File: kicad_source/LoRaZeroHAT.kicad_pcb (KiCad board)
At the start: 2 copper layers, 28 x 87 mm, 69 parts, among them J1 USB_B_Micro, J2 BM04B-SRSS-TB, Q1 NTR4171P, SW1 SW_Push, SW2 SW_Push, SW3 SW_SPDT, U1 RP2040, U2 Ai-Thinker-Ra-01, U3 NEO-M8N, U4 W25Q16JVSS, U5 24LC32, U6 BME280, U7 TPS3839DBZ, U8 TPS73630DBV, U9 MCP73832-2-OT, Y1 Crystal_GND24_Small

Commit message: connected schematic to layout
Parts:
- removed BT1: Battery_Cell, generationmake:KEYSTONE_1043
- removed C1, C11, C12, C2, C4, C5, C6, C7, C8, C9: 100 nF, Capacitor_SMD:C_0603_1608Metric
- removed C10, C15, C21, C22, C23, C3: 2.2 uF, Capacitor_SMD:C_0603_1608Metric
- removed C13, C14: 15 pF, Capacitor_SMD:C_0603_1608Metric
- removed D1, D3: LED_Small, LED_SMD:LED_0603_1608Metric
- removed D4: MBR120, Diode_SMD:D_SOD-123
- removed F1: SF-1206S050, Fuse:Fuse_1206_3216Metric
- removed J2: BM04B-SRSS-TB, Connector_JST:JST_SH_BM04B-SRSS-TB_1x04-1MP_P1.00mm_Vertical
- removed Q1: NTR4171P, Package_TO_SOT_SMD:SOT-23
- removed the R14 at (126.8, 123.5)
- removed the R15 at (136.5, 129.9)
- removed R16: 4k7, Resistor_SMD:R_0603_1608Metric
- removed SW1, SW2: SW_Push, Button_Switch_SMD:SW_Tactile_SPST_NO_Straight_CK_PTS636Sx25SMTRLFS
- removed SW3: SW_SPDT, Button_Switch_THT:SW_Slide-03_Wuerth-WS-SLTV_10x2.5x6.4_P2.54mm
- removed U1: RP2040, Package_DFN_QFN:QFN-56-1EP_7x7mm_P0.4mm_EP3.2x3.2mm
- removed U4: W25Q16JVSS, Package_SO:SOIC-8_5.23x5.23mm_P1.27mm
- removed U7: TPS3839DBZ, Package_TO_SOT_SMD:SOT-23
- removed U8: TPS73630DBV, Package_TO_SOT_SMD:SOT-23-5
- removed U9: MCP73832-2-OT, Package_TO_SOT_SMD:SOT-23-5
- removed Y1: Crystal_GND24_Small, Crystal:Crystal_SMD_3225-4Pin_3.2x2.5mm
- added CN1: RASPI-IO, generationmake:RASPI_ZERO_HAT_EDGE, F.Cu at (218.3, 96.8)
- added L2: Label, generationmake:generationmake_logo, F.Cu at (198.9, 130.3)
- added L3: Label, Symbol:OSHW-Symbol_6.7x6mm_SilkScreen, F.Cu at (219.4, 131.1)
- added L4: Label, generationmake:generationmake_small_solder, F.Cu at (222.2, 126.8)
- added R8: 0R, Resistor_SMD:R_0603_1608Metric, F.Cu at (213.6, 139.1)
- added R9: DNI, Resistor_SMD:R_0603_1608Metric, F.Cu at (213.6, 141.6)
- J1: value USB_B_Micro -> BM04B-SRSS-TB; footprint Connector_USB:USB_Micro-B_Molex_47346-0001 -> Connector_JST:JST_SH_BM04B-SRSS-TB_1x04-1MP_P1.00mm_Vertical
- R1: value 200R -> 0R
- R2: value 27R -> DNI
- R3: value 27R -> 10k
- R4, R5: value 1k -> 10k
- R6: value 1k -> DNI
- moved R7 89.9 mm to (213.6, 136.6), turned to 0 degrees
- moved R5 88.1 mm to (213.6, 131.6), turned to 0 degrees
- moved R1 79.7 mm to (213.6, 124.1)
- moved R13 79.0 mm to (213.6, 144.1), turned to 0 degrees
- moved R3 74.2 mm to (213.6, 129.1), turned to 0 degrees
- moved R2 72.8 mm to (213.6, 126.6), turned to 0 degrees
- moved R12 69.5 mm to (188.3, 157.4), turned to 0 degrees
- moved R6 66.8 mm to (213.6, 134.1), turned to 0 degrees
- moved R4 63.1 mm to (188.3, 154.9), turned to 0 degrees
- moved J1 49.4 mm to (190.7, 150.5)
- renumbered R9 to R14, R8 to R15
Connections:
- J1 pad 1: VBUS -> GND
- J1 pad 2: /RP2040/USB_DM -> +3V3
- J1 pad 3: /RP2040/USB_DP -> I2C_SDA
- J1 pad 4: unconnected-(J1-ID-Pad4) -> I2C_SCL
- R1 pad 1: +3V3 -> /RaspberryPiZeroHAT/SPI_CE0
- R1 pad 2: /RP2040/ADC_AVDD -> LORA_CS
- R13 pad 1: +3V3 -> SPI_MISO
- R13 pad 2: I2C_SDA -> GND
- R2 pad 1: /RP2040/USB_DP -> LORA_CS
- R2 pad 2: /RP2040/USB_DPX -> /RaspberryPiZeroHAT/SPI_CE1
- R3 pad 1: /RP2040/USB_DM -> +3.3V
- R3 pad 2: /RP2040/USB_DMX -> LORA_CS
- R4 pad 1: /RP2040/XR -> +3V3
- R4 pad 2: /RP2040/XOUT -> I2C_SDA
- R5 pad 1: /RP2040/GPIO25 -> +3.3V
- R5 pad 2: /RP2040/D1_R -> LORA_INT
- R6 pad 1: Net-(R6-Pad1) -> /RaspberryPiZeroHAT/INTERRUPT_23
- R6 pad 2: /RP2040/QSPI_SS -> LORA_INT
- R7 pad 1: /RP2040/LORA_DIO0_R -> /RaspberryPiZeroHAT/INTERRUPT_24
- R7 pad 2: LORA_DIO0 -> LORA_INT
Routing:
- net (no net): track 0.00 -> 291.4 mm, vias 0 -> 11
- net /RP2040/LORA_DIO0_R: track 35.6 -> 0.00 mm
- net VBUS: track 33.8 -> 0.00 mm, vias 2 -> 0
- net +1V1: track 26.1 -> 0.00 mm, vias 3 -> 0
- net /RP2040/QSPI_SS: track 16.9 -> 0.00 mm
- net /RP2040/QSPI_SD1: track 14.7 -> 0.00 mm
- net VCC: track 14.0 -> 0.00 mm
- net /RP2040/QSPI_SD2: track 13.5 -> 0.00 mm
- net /RP2040/GPIO25: track 11.9 -> 0.00 mm
- net +BATT: track 10.2 -> 0.00 mm
- net /RP2040/USB_DPX: track 9.98 -> 0.00 mm
- net /RP2040/XIN: track 9.95 -> 0.00 mm
- net /RP2040/RUN: track 9.76 -> 0.00 mm
- net /RP2040/USB_DMX: track 9.17 -> 0.00 mm
- net Net-(U9-STAT): track 8.05 -> 0.00 mm
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
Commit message: made first connections
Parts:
- removed H1, H2, H3: MountingHole, MountingHole:MountingHole_2.2mm_M2
- moved R11 117.5 mm to (246.7, 115.8), turned to 180 degrees
- moved C17 116.8 mm to (246.7, 114.3), turned to 180 degrees
- moved U5 115.4 mm to (247.0, 109.0), turned to -90 degrees
- moved C16 112.5 mm to (246.1, 102.2), turned to 90 degrees
- moved U3 97.3 mm to (237.7, 109.9), turned to 0 degrees
- moved U2 88.3 mm to (212.4, 114.1), turned to 0 degrees
- moved AE2 87.7 mm to (229.3, 120.1), turned to -90 degrees
- moved AE1 85.7 mm to (197.5, 120.8), turned to -90 degrees
- moved L1 84.6 mm to (229.3, 116.2), turned to -90 degrees
- moved C19 82.9 mm to (206.7, 104.2), turned to 180 degrees
- moved R14 82.4 mm to (229.3, 112.9), turned to -90 degrees
- moved R10 80.8 mm to (229.3, 109.8), turned to 90 degrees
- moved C18 80.8 mm to (206.7, 102.6), turned to 180 degrees
- moved R15 79.7 mm to (229.3, 106.7), turned to 90 degrees
- moved D2 79.1 mm to (229.3, 103.6), turned to -90 degrees
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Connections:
- C16 pad 1: +3V3 -> +3.3V
- C17 pad 1: +3V3 -> +3.3V
- C18 pad 1: +3V3 -> +3.3V
- C19 pad 1: +3V3 -> +3.3V
- C20 pad 1: +3V3 -> +3.3V
- CN1 pad 23: SPI_CLK -> SPI_SCK
- CN1 pad 29: unconnected-(CN1-BCM5-Pad29) -> LORA_DIO0
- CN1 pad 31: unconnected-(CN1-BCM6-Pad31) -> LORA_RESET
- J1 pad 2: +3V3 -> +3.3V
- R12 pad 1: +3V3 -> +3.3V
- R4 pad 1: +3V3 -> +3.3V
- U2 pad 3: +3V3 -> +3.3V
- U3 pad 23: +3V3 -> +3.3V
- U5 pad 8: +3V3 -> +3.3V
- U6 pad 2: +3V3 -> +3.3V
- U6 pad 6: +3V3 -> +3.3V
- U6 pad 8: +3V3 -> +3.3V
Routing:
- net (no net): track 291.4 -> 0.00 mm, vias 11 -> 0
- net GND: track 520.0 -> 232.4 mm, vias 45 -> 13
- net +3V3: track 171.1 -> 0.00 mm, vias 13 -> 0
- net +3.3V: track 0.00 -> 101.5 mm, vias 0 -> 2
- net LORA_CS: track 56.2 -> 11.0 mm
- net LORA_RESET: track 79.7 -> 35.6 mm, vias 2 -> 1
- net SPI_MOSI: track 52.0 -> 15.5 mm, vias 2 -> 0
- net SERIAL_TX: track 43.8 -> 8.31 mm
- net SERIAL_RX: track 44.4 -> 9.70 mm
- net SPI_MISO: track 42.6 -> 25.4 mm
- net SPI_SCK: track 40.5 -> 24.2 mm
- net LORA_DIO0: track 47.1 -> 35.1 mm, vias 0 -> 1
- net /LoRa GNSS/LORA_ANTENNA: track 8.90 -> 18.1 mm
- net /RaspberryPiZeroHAT/SPI_CE1: track 0.00 -> 8.35 mm
- net /RaspberryPiZeroHAT/SPI_CE0: track 0.00 -> 8.06 mm
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- removed copper zone on B.Cu, net GND
- removed copper zone on F.Cu, net GND
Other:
- board outline removed

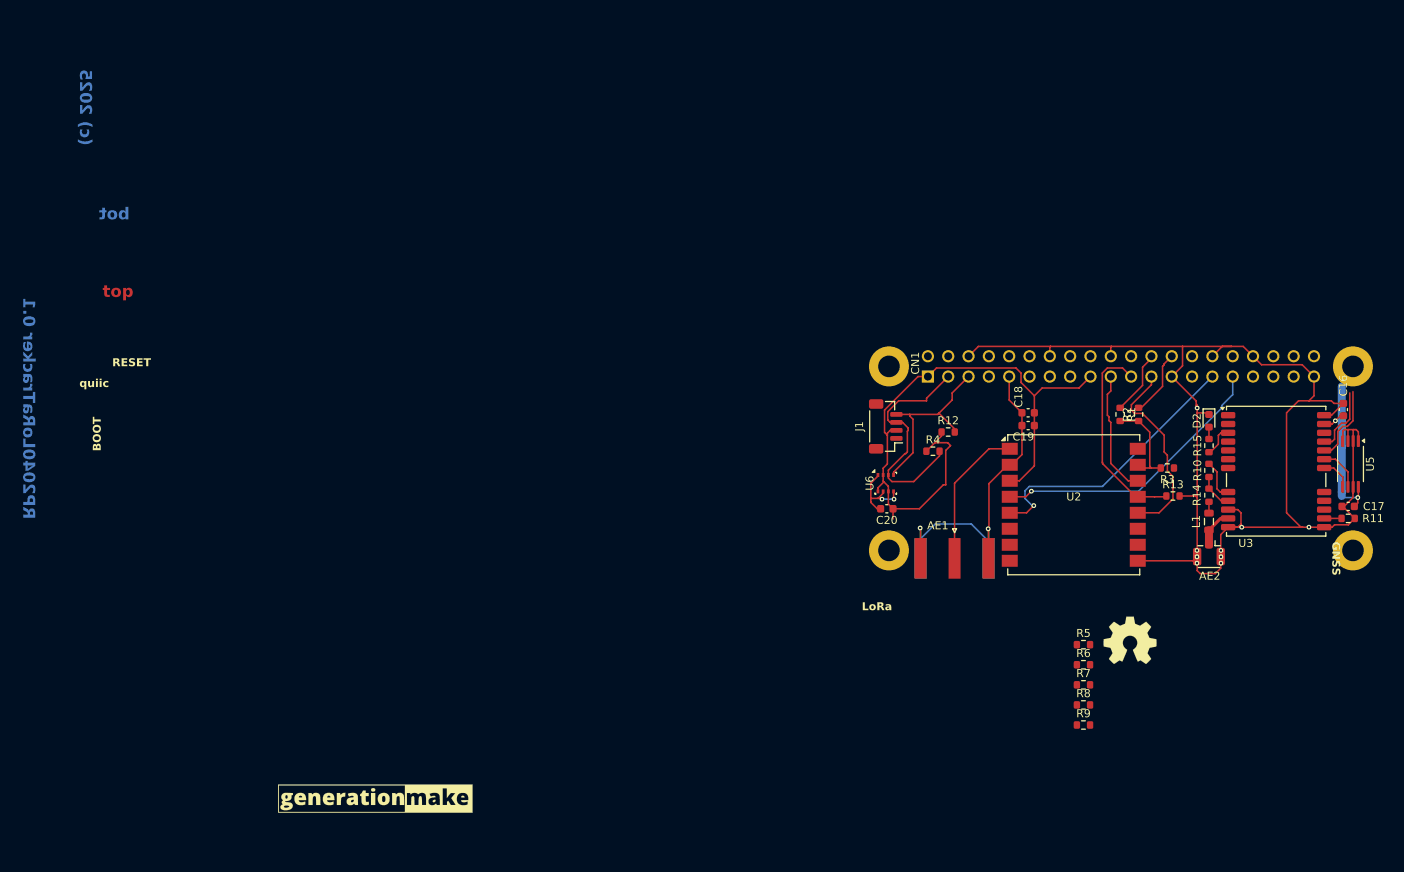
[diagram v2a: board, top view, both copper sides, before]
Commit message: updated layout
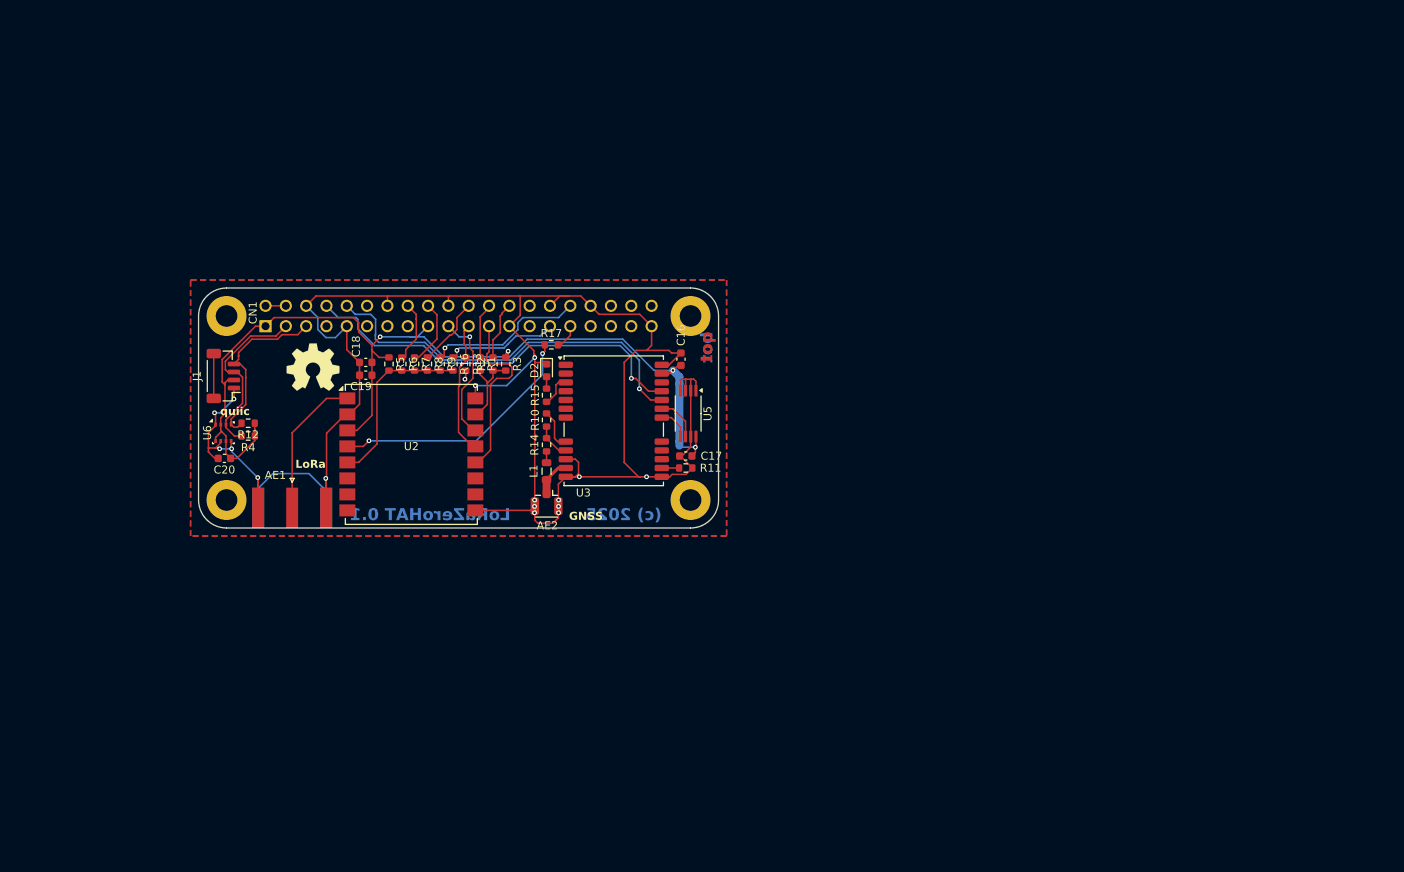
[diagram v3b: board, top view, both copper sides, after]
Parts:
- removed FID1: Fiducial, generationmake:generationmake_small_solder
- removed FID2: Fiducial, generationmake:generationmake_logo
- removed L2: Label, generationmake:generationmake_logo
- removed L3: Label, Symbol:OSHW-Symbol_6.7x6mm_SilkScreen
- removed L4: Label, generationmake:generationmake_small_solder
- added L5: Label, Symbol:OSHW-Symbol_6.7x6mm_SilkScreen, F.Cu at (117.3, 96.9)
- added L6: Label, generationmake:generationmake_small_solder, F.Cu at (115.0, 101.0)
- added L7: Label, generationmake:generationmake_logo, B.Cu at (136.2, 110.3)
- added R16: DNI, Resistor_SMD:R_0603_1608Metric, F.Cu at (134.8, 96.5)
- added R17: 0R, Resistor_SMD:R_0603_1608Metric, F.Cu at (147.1, 94.1)
- moved R5 93.6 mm to (126.8, 96.5), turned to -90 degrees
- moved R6 93.1 mm to (128.4, 96.5), turned to -90 degrees
- moved R7 92.7 mm to (130.0, 96.5), turned to -90 degrees
- moved R8 92.4 mm to (131.6, 96.5), turned to -90 degrees
- moved R9 92.2 mm to (133.2, 96.5), turned to -90 degrees
- moved R13 89.9 mm to (136.4, 96.5), turned to -90 degrees
- moved R12 87.5 mm to (109.2, 103.9), turned to 180 degrees
- moved R4 85.6 mm to (109.2, 105.5), turned to 180 degrees
- moved R3 83.7 mm to (141.4, 96.5), turned to -90 degrees
- moved AE2 83.0 mm to (146.5, 113.8)
- moved CN1 83.0 mm to (135.5, 90.5)
- moved D2 83.0 mm to (146.5, 97.3)
- moved J1 83.0 mm to (106.1, 98.0)
- moved L1 83.0 mm to (146.5, 109.9)
- moved R10 83.0 mm to (146.5, 103.5)
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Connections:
- CN1 pad 29: LORA_DIO0 -> /RaspberryPiZeroHAT/INTERRUPT_5
- CN1 pad 31: LORA_RESET -> /RaspberryPiZeroHAT/LORA_RESET_R
- U2 pad 5: LORA_DIO0 -> LORA_INT
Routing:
- net SERIAL_TX: track 8.31 -> 50.4 mm, vias 0 -> 1
- net SERIAL_RX: track 9.70 -> 49.7 mm, vias 0 -> 1
- net LORA_DIO0: track 35.1 -> 0.00 mm, vias 1 -> 0
- net GND: track 232.4 -> 260.9 mm, vias 13 -> 17
- net +3.3V: track 101.5 -> 124.7 mm, vias 2 -> 4
- net LORA_INT: track 0.00 -> 22.5 mm
- net /RaspberryPiZeroHAT/INTERRUPT_12: track 0.00 -> 19.6 mm, vias 0 -> 1
- net /RaspberryPiZeroHAT/INTERRUPT_5: track 0.00 -> 13.8 mm, vias 0 -> 1
- net /RaspberryPiZeroHAT/INTERRUPT_25: track 0.00 -> 8.50 mm
- net SPI_MISO: track 25.4 -> 17.1 mm
- net /RaspberryPiZeroHAT/INTERRUPT_24: track 0.00 -> 7.86 mm
- net /RaspberryPiZeroHAT/INTERRUPT_23: track 0.00 -> 7.43 mm
- net I2C_SDA: track 29.4 -> 22.5 mm
- net unconnected-(J1-MountPin-PadMP): track 0.00 -> 5.60 mm
- net LORA_RESET: track 35.6 -> 31.9 mm, vias 1 -> 2
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- added copper zone on B.Cu, net GND
- added copper zone on F.Cu, net GND
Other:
- board outline added: 65 x 30 mm
- board text added: "LoRaZeroHAT 0.1"
- board text removed: "BOOT"
- board text removed: "RESET"
- board text removed: "RP2040LoRaTracker 0.1"

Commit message: schaltplan neu annotiert
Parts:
- renumbered AE2 to AE1, AE1 to AE2, C16 to C1, C17 to C2, C20 to C3, C18 to C4, C19 to C5, D2 to D1, L5 to L1, L6 to L2, L7 to L3, L1 to L4, R13 to R1, R2 to R10, R3 to R11, R10 to R12, R11 to R13, R4 to R15, R15 to R16, R12 to R17, R17 to R2, R16 to R3, R6 to R4, R7 to R5, R8 to R6, R9 to R7, R5 to R8, R1 to R9, U5 to U1, U3 to U2, U2 to U3, U6 to U4

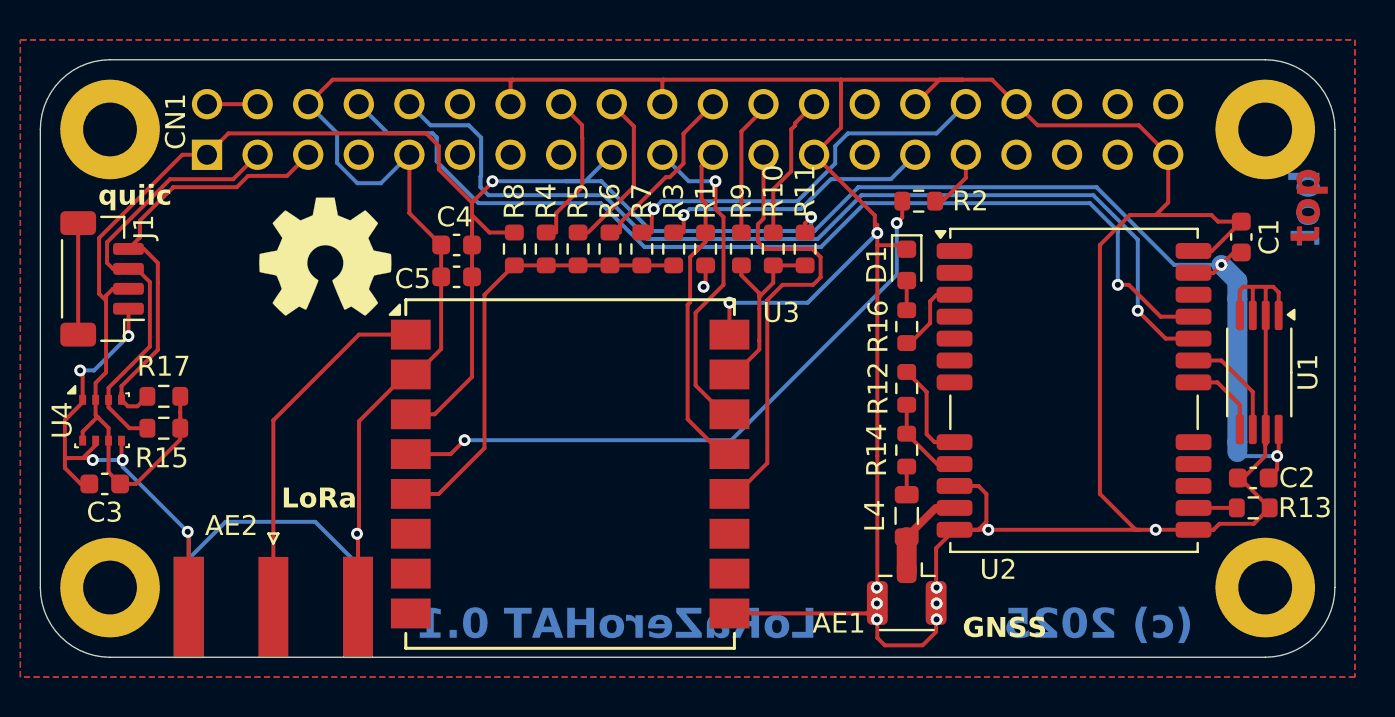
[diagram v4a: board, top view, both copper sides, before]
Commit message: updated DRC
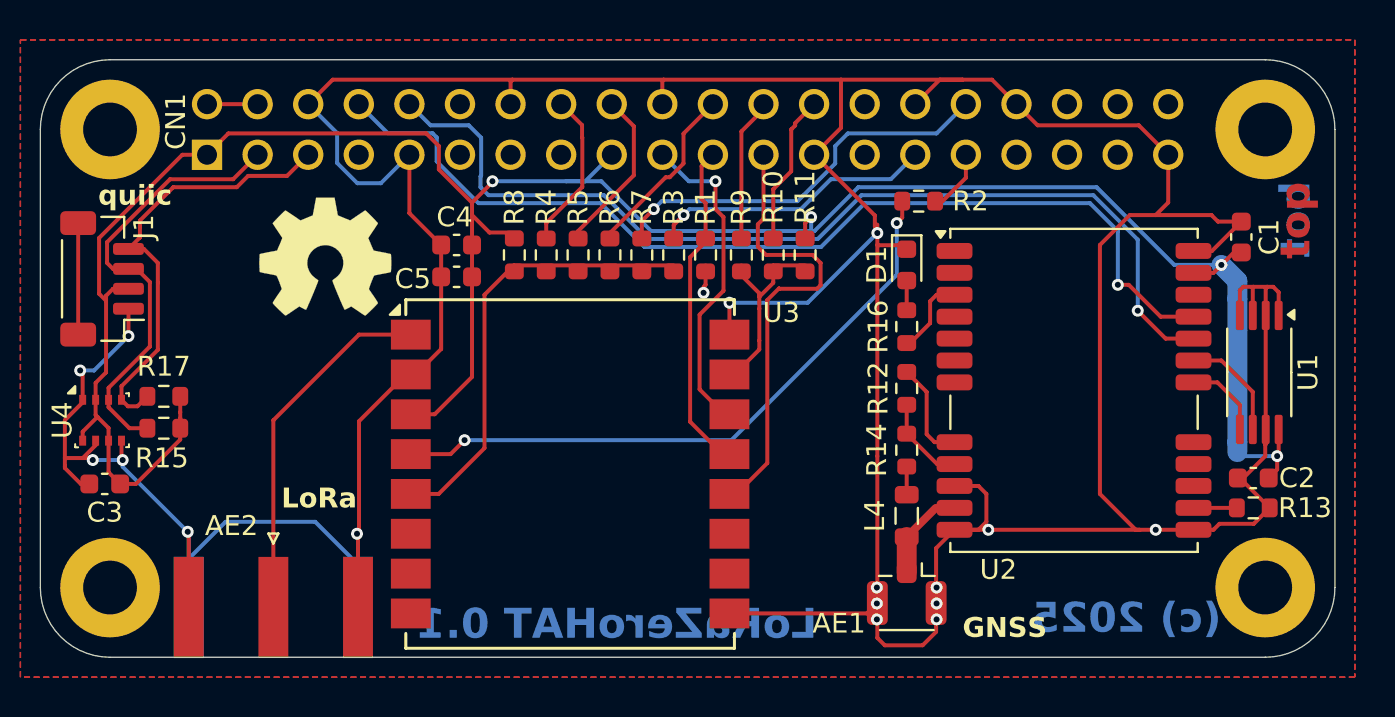
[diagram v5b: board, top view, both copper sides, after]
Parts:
- moved R1 0.30 mm to (136.4, 96.8)
- moved R10 0.30 mm to (139.8, 96.8)
- moved R11 0.30 mm to (141.4, 96.8)
- moved R3 0.30 mm to (134.8, 96.8)
- moved R4 0.30 mm to (128.4, 96.8)
- moved R5 0.30 mm to (130.0, 96.8)
- moved R6 0.30 mm to (131.6, 96.8)
- moved R7 0.30 mm to (133.2, 96.8)
- moved R8 0.30 mm to (126.8, 96.8)
- moved R9 0.30 mm to (138.2, 96.8)
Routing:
- net I2C_SCL: track 23.1 -> 22.5 mm
